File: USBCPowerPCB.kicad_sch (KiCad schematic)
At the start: 5 parts, among them J1 USB_C_Receptacle_USB2.0_16P, J2 5V_OUT, J3 12V_OUT

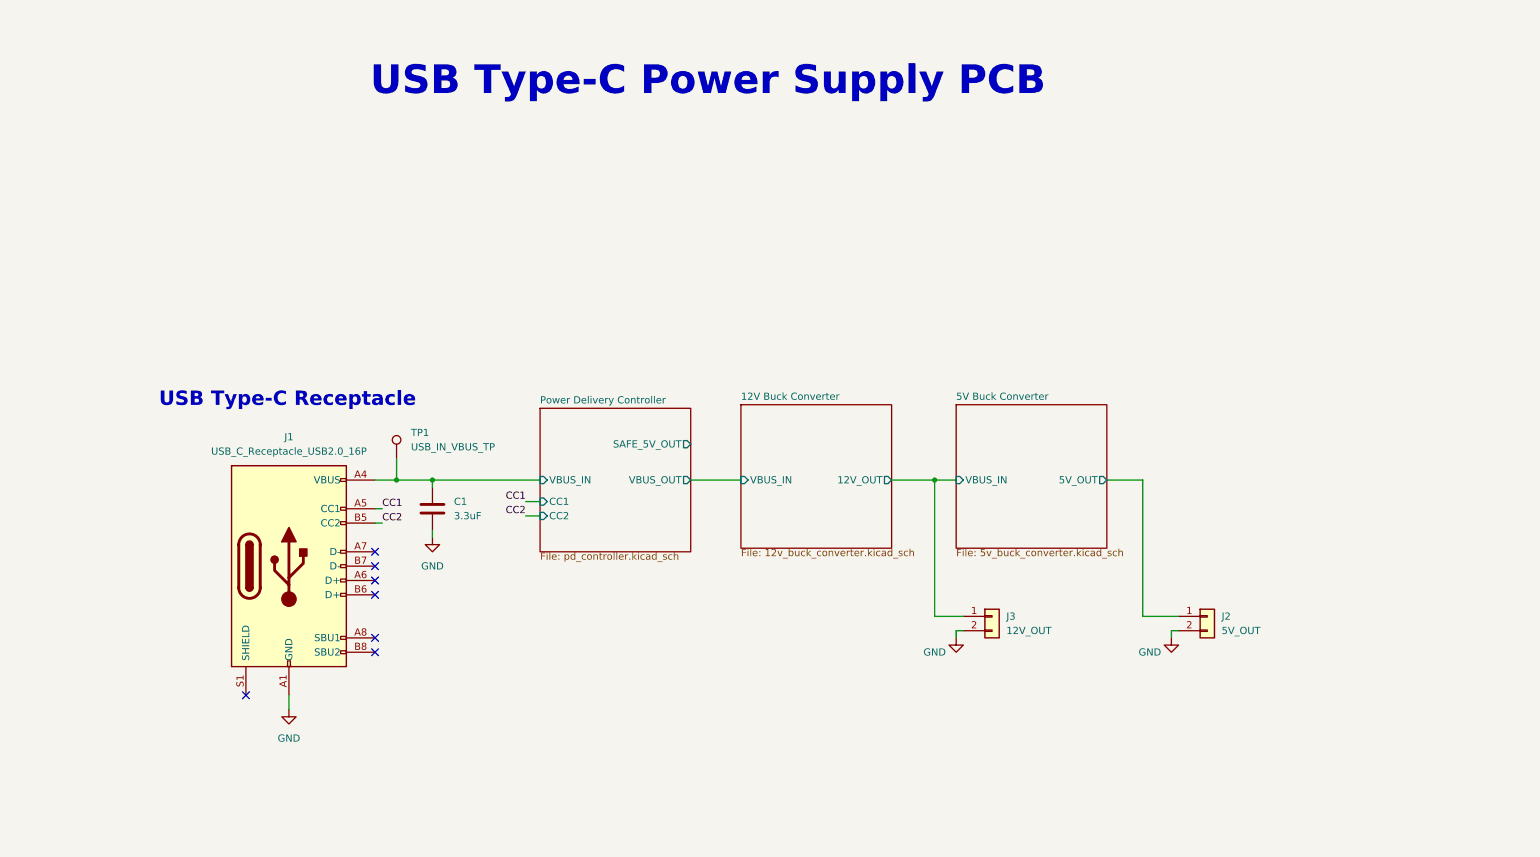
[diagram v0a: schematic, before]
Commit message: almost done w/ schematic, just need to finish footprint assignment (make sure buck converter components are correctly chosen and there aren't caps that need to be different and stuff)
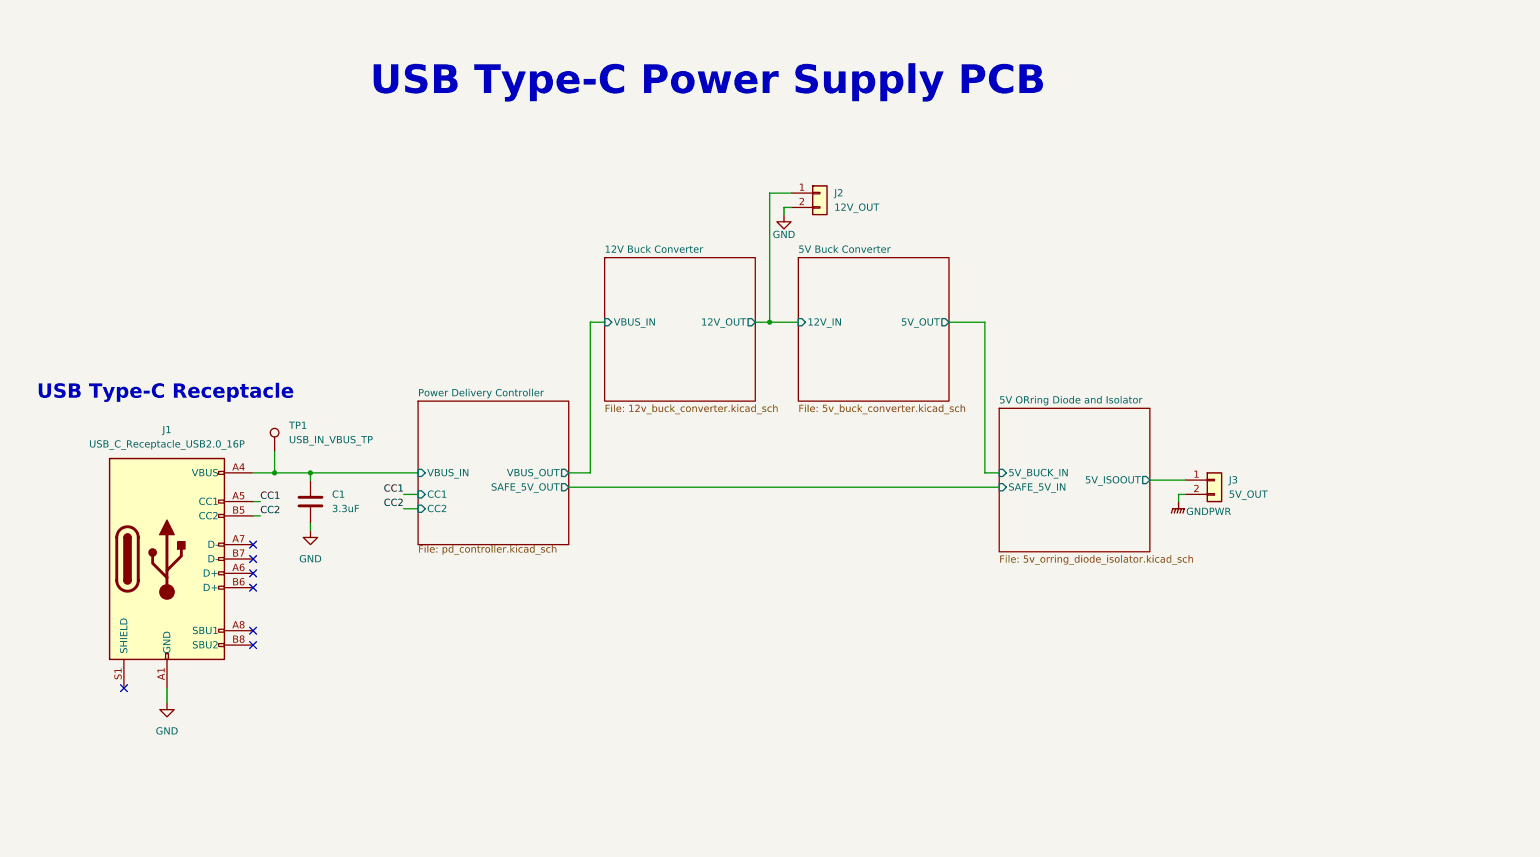
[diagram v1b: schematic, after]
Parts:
- removed J2: 5V_OUT, symbol Connector_Generic:Conn_01x02
- added J3: 5V_OUT, symbol Connector_Generic:Conn_01x02
- renumbered J3 to J2
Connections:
- new net 5V ORring Diode and Isolator/5V_ISOOUT: J3.1 (Pin_1)
- new net GNDPWR: J3.2 (Pin_2)
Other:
- added sheet 5V ORring Diode and Isolator (5v_orring_diode_isolator.kicad_sch)
- sheet 5V Buck Converter ports: added 12V_IN; removed VBUS_IN
- moved on the sheet: C1, J1, J2, TP1

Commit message: cleaned up schematic, added power LEDs and testpoints
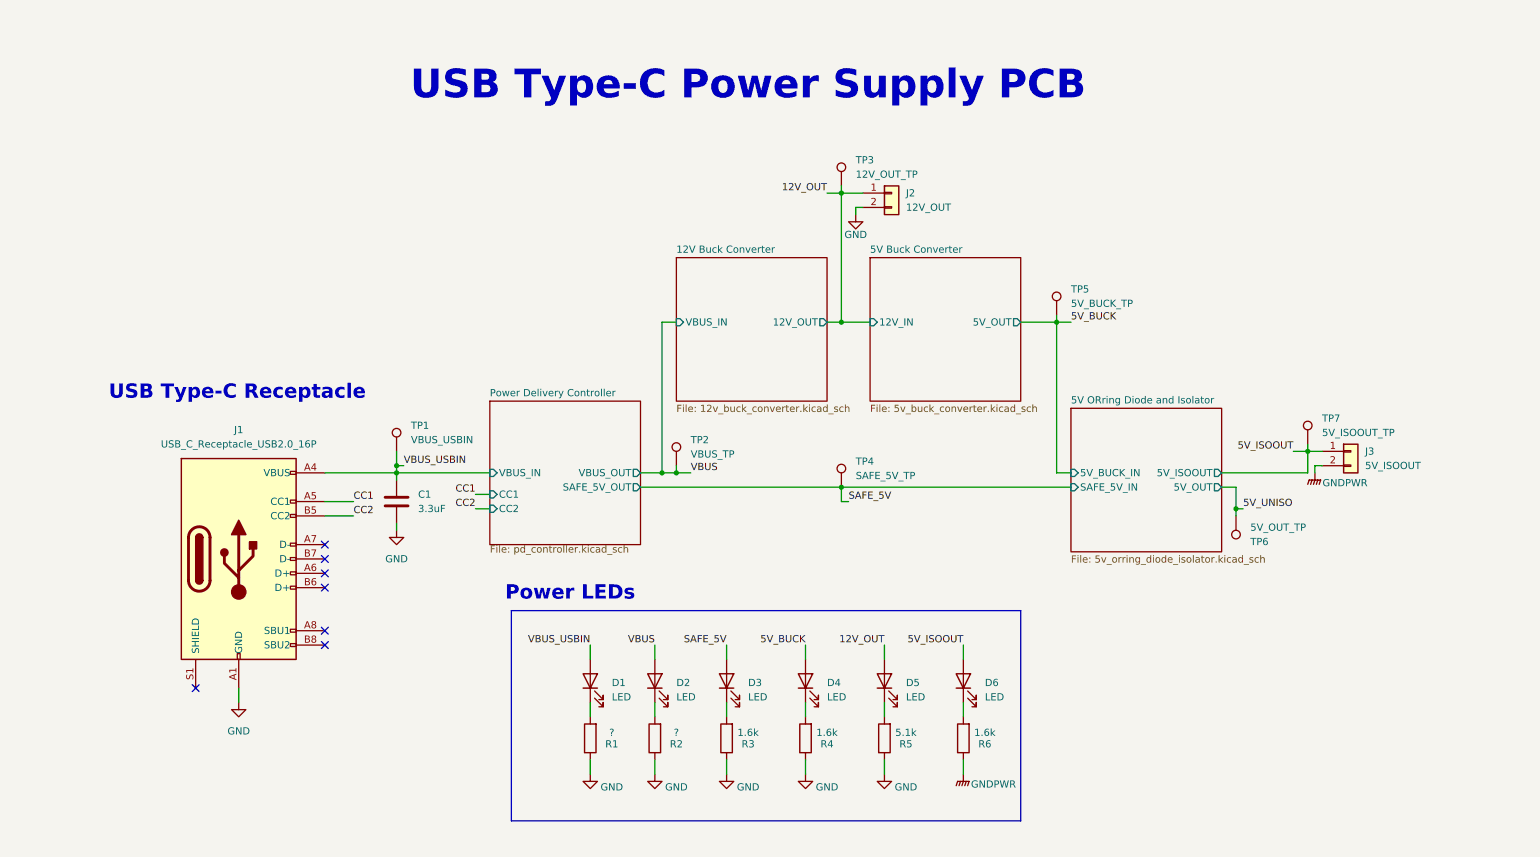
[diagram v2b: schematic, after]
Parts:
- added D1, D2, D3, D4, D5, D6: LED, LED_SMD:LED_0805_2012Metric, symbol Device:LED
- added R1, R2: ?, Resistor_SMD:R_0805_2012Metric, symbol Device:R
- added R3, R4, R6: 1.6k, Resistor_SMD:R_0805_2012Metric, symbol Device:R
- added R5: 5.1k, Resistor_SMD:R_0805_2012Metric, symbol Device:R
- added TP2: VBUS_TP, TestPoint:TestPoint_Pad_D2.5mm, symbol Connector:TestPoint
- added TP3: 12V_OUT_TP, TestPoint:TestPoint_Pad_D2.5mm, symbol Connector:TestPoint
- added TP4: SAFE_5V_TP, TestPoint:TestPoint_Pad_D2.5mm, symbol Connector:TestPoint
- added TP5: 5V_BUCK_TP, TestPoint:TestPoint_Pad_D2.5mm, symbol Connector:TestPoint
- added TP6: 5V_OUT_TP, TestPoint:TestPoint_Pad_D2.5mm, symbol Connector:TestPoint
- added TP7: 5V_ISOOUT_TP, TestPoint:TestPoint_Pad_D2.5mm, symbol Connector:TestPoint
- J3: value 5V_OUT -> 5V_ISOOUT
- TP1: value USB_IN_VBUS_TP -> VBUS_USBIN
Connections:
- net GND: now also R1.1, R2.1, R3.1, R4.1, R5.1
- net GNDPWR: now also R6.1
- net 12V Buck Converter/12V_OUT renamed 12V_OUT
- net 12V_OUT: now also D5.2 (A), TP3.1
- net 5V ORring Diode and Isolator/5V_ISOOUT renamed 5V_ISOOUT
- net 5V_ISOOUT: now also D6.2 (A), TP7.1
- net Power Delivery Controller/VBUS_IN renamed VBUS_USBIN
- net VBUS_USBIN: now also D1.2 (A)
- new net: D3.1 (K), R3.2
- new net: D1.1 (K), R1.2
- new net: D5.1 (K), R5.2
- new net: D6.1 (K), R6.2
- new net: D4.1 (K), R4.2
- new net: D2.1 (K), R2.2
- new net 5V_BUCK: D4.2 (A), TP5.1
- new net 5V_UNISO: TP6.1
- new net SAFE_5V: D3.2 (A), TP4.1
- new net VBUS: D2.2 (A), TP2.1
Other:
- sheet 5V ORring Diode and Isolator ports: added 5V_OUT; removed none
- note added: "Power LEDs"
- moved on the sheet: C1, J1, J2, J3, TP1

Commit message: finished footprint assignment
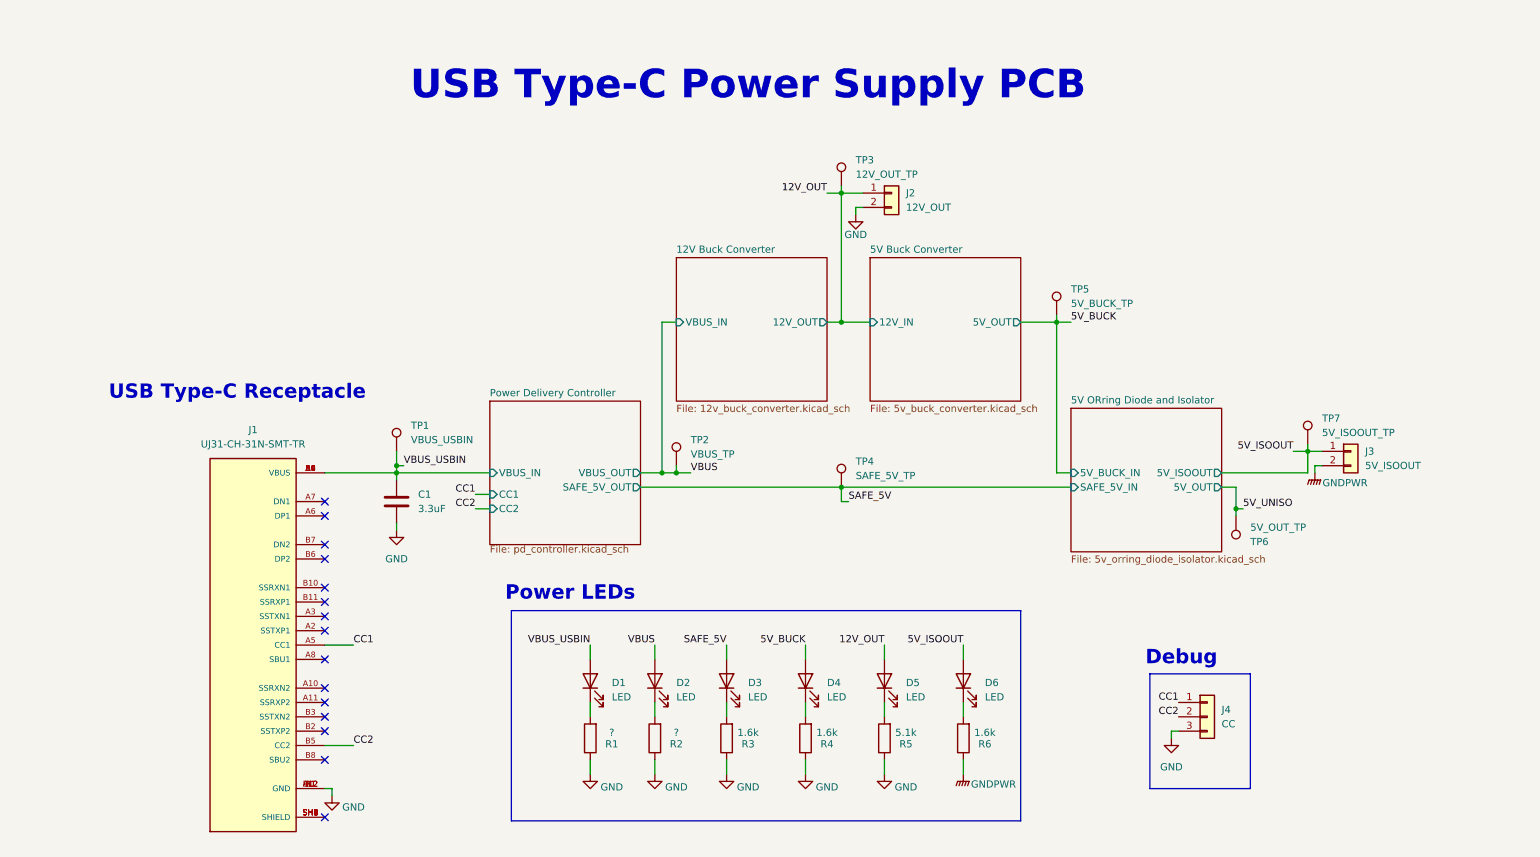
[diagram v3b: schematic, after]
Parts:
- removed J1: USB_C_Receptacle_USB2.0_16P, symbol Connector:USB_C_Receptacle_USB2.0_16P
- added J1: UJ31-CH-31N-SMT-TR, UTSVT_Connectors:CUI_UJ31-CH-31N-SMT-TR, symbol utsvt-connectors:UJ31-CH-31N-SMT-TR
- added J4: CC, Connector_PinHeader_2.54mm:PinHeader_1x03_P2.54mm_Vertical, symbol Connector_Generic:Conn_01x03
- J2, J3: footprint (none) -> Connector:Banana_Jack_2Pin
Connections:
- net CC1: now also J1.A5 (CC1), J4.1 (Pin_1)
- net CC2: now also J1.B5 (CC2), J4.2 (Pin_2)
- net GND: now also J1.A1 (GND), J1.A12 (GND), J1.B1 (GND), J1.B12 (GND), J4.3 (Pin_3)
- net VBUS_USBIN: now also J1.A4 (VBUS), J1.A9 (VBUS), J1.B4 (VBUS), J1.B9 (VBUS)
- new net: J1.SH1 (SHIELD), J1.SH2 (SHIELD), J1.SH3 (SHIELD), J1.SH4 (SHIELD), J1.SH5 (SHIELD), J1.SH6 (SHIELD)
- no-connect marks 7 -> 15
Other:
- note added: "Debug"

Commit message: added protection diodes
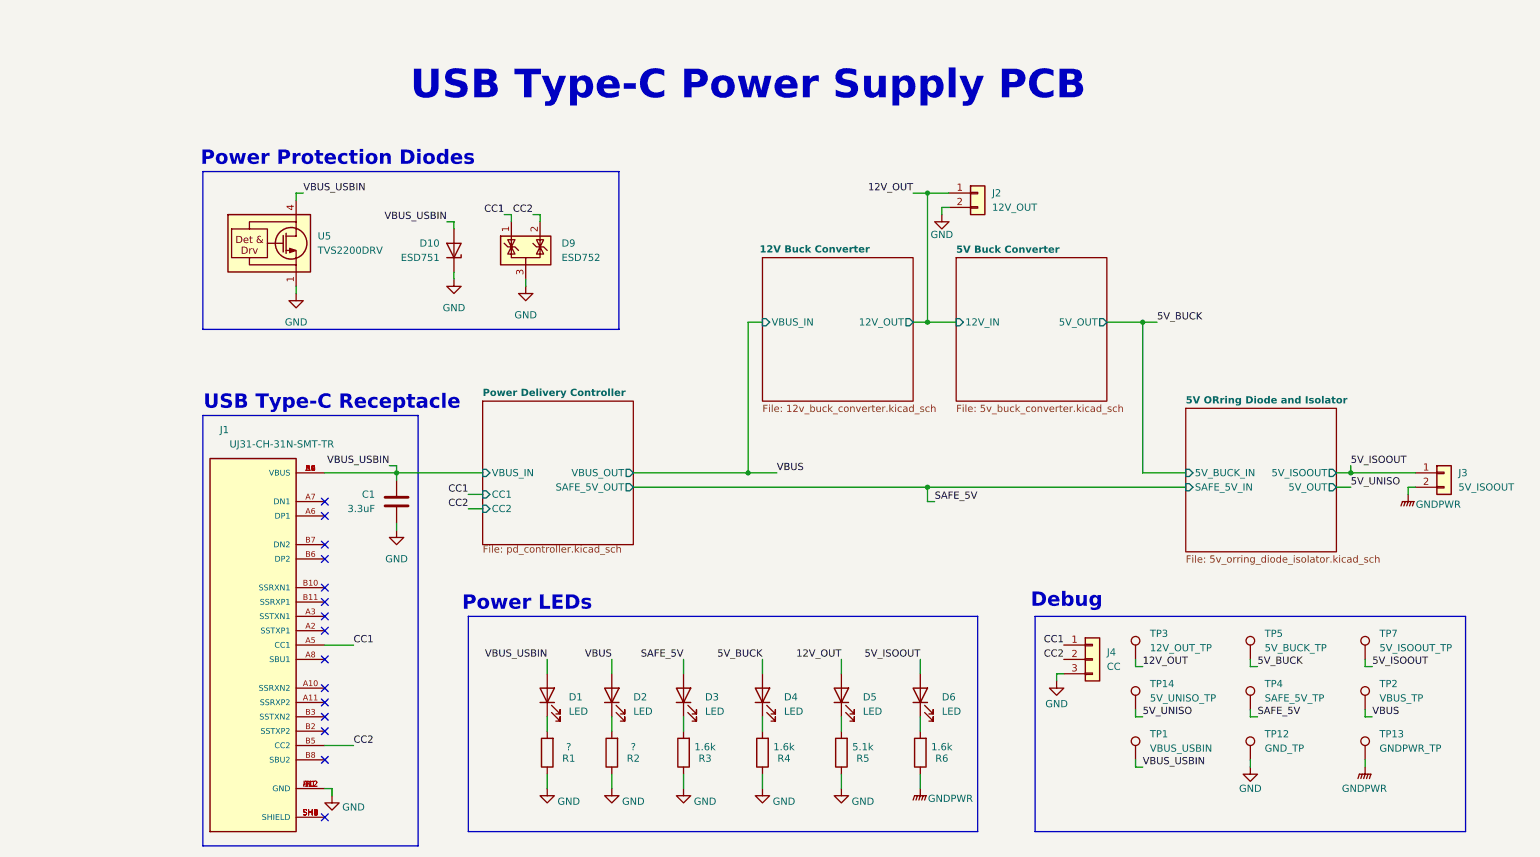
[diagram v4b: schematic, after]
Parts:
- removed TP6: 5V_OUT_TP, TestPoint:TestPoint_Pad_D2.5mm, symbol Connector:TestPoint
- added D10: ESD751, Diode_SMD:D_SOD-523, symbol Diode:ESD5Zxx
- added D9: ESD752, Package_TO_SOT_SMD:SOT-23, symbol Power_Protection:NUP2105L
- added TP12: GND_TP, TestPoint:TestPoint_Pad_D2.5mm, symbol Connector:TestPoint
- added TP13: GNDPWR_TP, TestPoint:TestPoint_Pad_D2.5mm, symbol Connector:TestPoint
- added TP14: 5V_UNISO_TP, TestPoint:TestPoint_Pad_D2.5mm, symbol Connector:TestPoint
- added U5: TVS2200DRV, Package_SON:WSON-6-1EP_2x2mm_P0.65mm_EP1x1.6mm, symbol Power_Protection:TVS2200DRV
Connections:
- net 5V_UNISO: now also TP14.1
- net CC1: now also D9.1 (K)
- net CC2: now also D9.2 (K)
- net GND: now also D10.1 (K), D9.3 (A), TP12.1, U5.1 (GND), U5.2 (GND), U5.3 (GND), U5.7 (GND)
- net GNDPWR: now also TP13.1
- net VBUS_USBIN: now also D10.2 (A), U5.4 (IN), U5.5 (IN), U5.6 (IN)
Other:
- note added: "Power Protection Diodes"
- moved on the sheet: D1, D2, D3, D4, D5, D6, J2, J3, J4, R1, R2, R3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

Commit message: address review changes, add more output protections
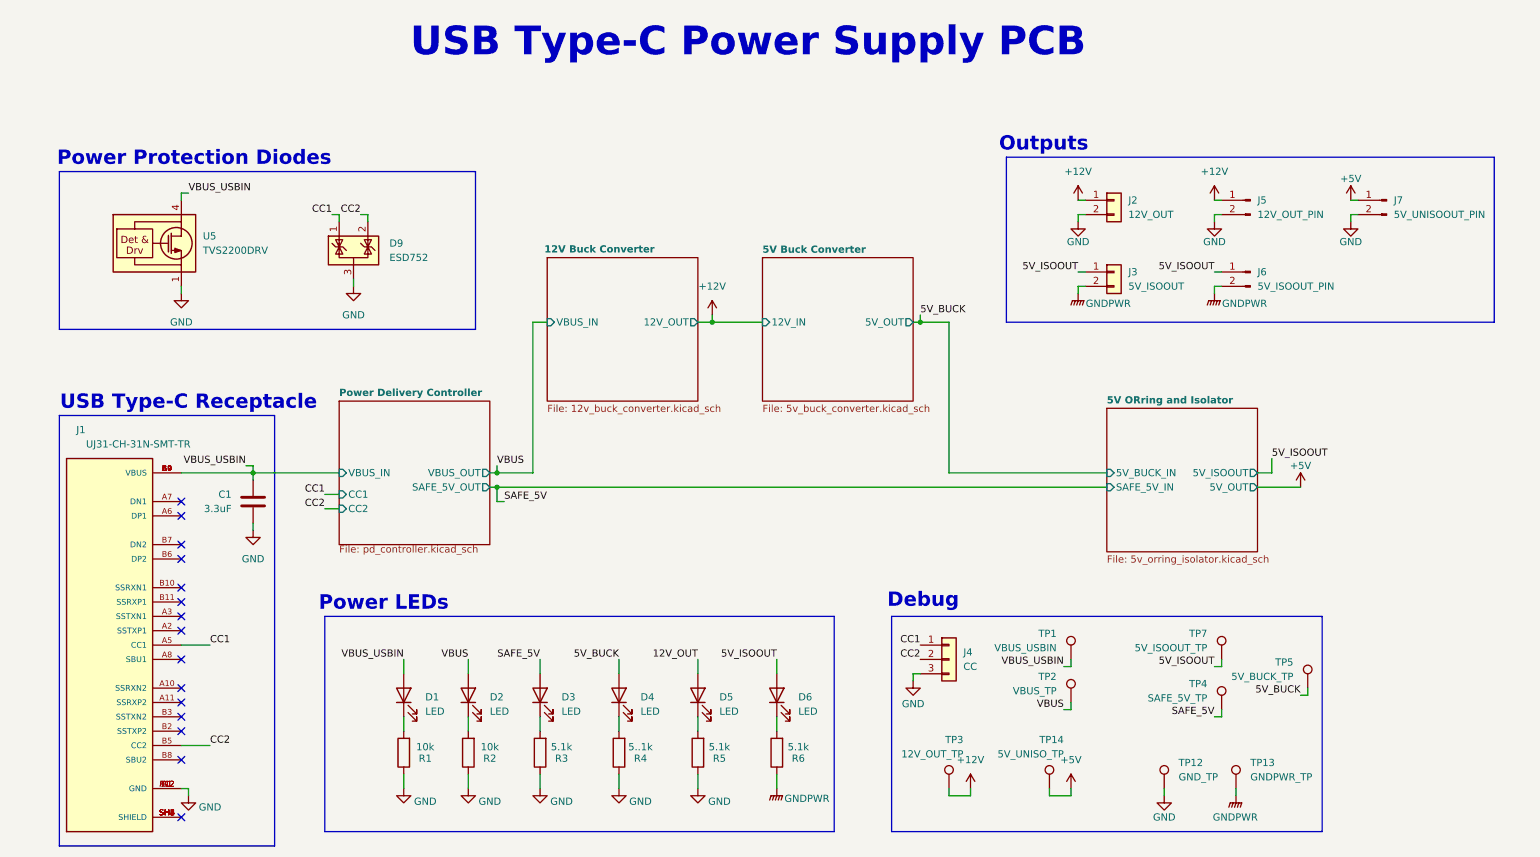
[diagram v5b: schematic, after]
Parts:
- removed D10: ESD751, Diode_SMD:D_SOD-523, symbol Diode:ESD5Zxx
- added J5: 12V_OUT_PIN, symbol Connector:Conn_01x02_Pin
- added J6: 5V_ISOOUT_PIN, symbol Connector:Conn_01x02_Pin
- added J7: 5V_UNISOOUT_PIN, symbol Connector:Conn_01x02_Pin
- J2, J3: footprint Connector:Banana_Jack_2Pin -> (none)
- R1, R2: value ? -> 10k
- R3, R6: value 1.6k -> 5.1k
- R4: value 1.6k -> 5..1k
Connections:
- net 12V_OUT: no longer J2.1 (Pin_1), TP3.1
- net 5V_ISOOUT: now also J6.1 (Pin_1)
- net GND: now also J5.2 (Pin_2), J7.2 (Pin_2)
- net GNDPWR: now also J6.2 (Pin_2)
- net 5V_UNISO renamed +5V
- net +5V: now also J7.1 (Pin_1)
- new net +12V: J2.1 (Pin_1), J5.1 (Pin_1), TP3.1
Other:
- sheet 5V ORring Diode and Isolator renamed 5V ORring and Isolator
- sheet 5V ORring and Isolator: file 5v_orring_diode_isolator.kicad_sch -> 5v_orring_isolator.kicad_sch
- note added: "Outputs"
- moved on the sheet: C1, D1, D2, D3, D4, D5, D6, D9, J1, J4, R1, R2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

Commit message: footprint assignment again
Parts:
- J3: renamed from J2; footprint (none) -> UTSVT_Connectors:Molex_MicroFit3.0_1x2xP3.00mm_PolarizingPeg_Vertical
- J4: renamed from J3; footprint (none) -> UTSVT_Connectors:Molex_MicroFit3.0_1x2xP3.00mm_PolarizingPeg_Vertical
- J5, J6, J7: footprint (none) -> Connector_PinHeader_2.54mm:PinHeader_1x02_P2.54mm_Vertical
- renumbered D9 to D1, D1 to D2, D2 to D3, D3 to D4, D4 to D5, D5 to D6, D6 to D7, J4 to J2, TP3 to TP1, TP14 to TP2, TP1 to TP3, TP2 to TP4, TP12 to TP5, TP7 to TP6, TP4 to TP7, TP13 to TP8, TP5 to TP9, U5 to U1
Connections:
- net 12V_OUT is gone; now on net +5V: D6.2 (A)
- net +12V: now also D5.2 (A)
- net 5V_BUCK: no longer D5.2 (A)
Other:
- moved on the sheet: D4, R3
